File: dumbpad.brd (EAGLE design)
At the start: 97 x 78.5 mm, 41 parts

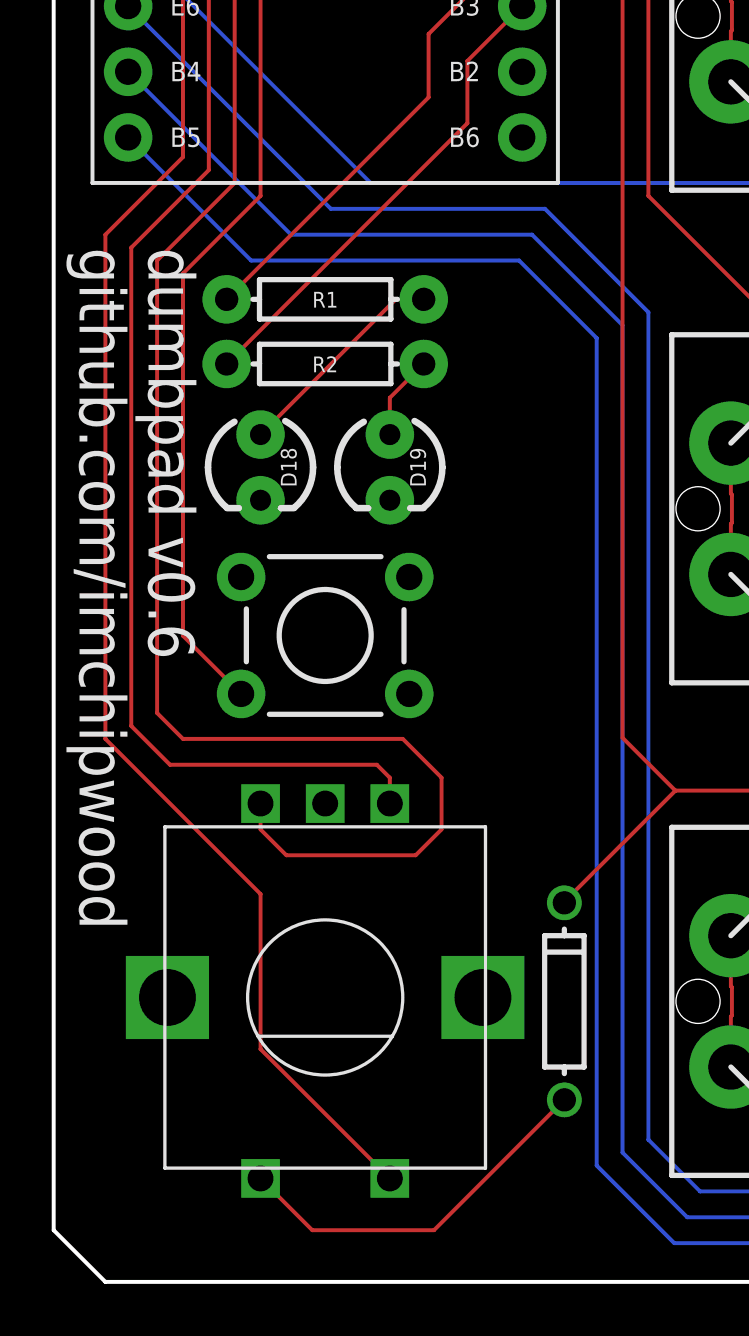
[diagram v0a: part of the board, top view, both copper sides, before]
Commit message: added jumpers for reversing encoder when using encoder on right side instead of left
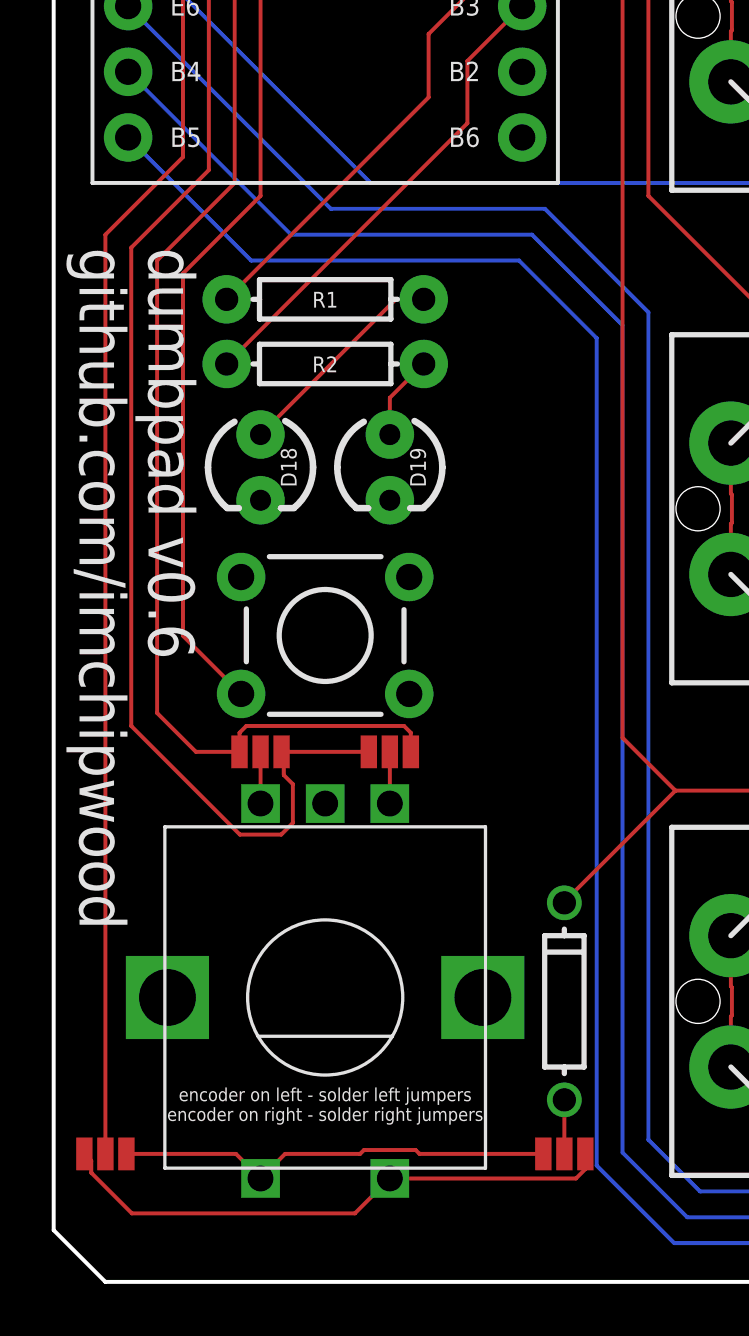
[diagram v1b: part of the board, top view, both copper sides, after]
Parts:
- added JP1, JP2, JP3, JP4: JUMPER-SMT_3_NO_NO-SILK, SparkFun-Jumpers:SMT-JUMPER_3_NO_NO-SILK
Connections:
- removed net N$10: D17.A, RE1.E
- new net ENCODER_A_B: JP3.2, RE1.A
- new net ENCODER_B_A: JP4.2, RE1.B
- new net ROW3_A: D17.A, JP1.2
- new net S17_D: JP1.1, JP2.3, RE1.D
- new net S17_E: JP1.3, JP2.1, RE1.E
- net COL0: now also JP2.2; no longer RE1.D
- net ENCODER_L0: now also JP3.1, JP4.1; no longer RE1.A
- net ENCODER_L1: now also JP3.3, JP4.3; no longer RE1.B
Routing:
- net S17_D: track 0.00 -> 21.9 mm
- net S17_E: track 0.00 -> 17.0 mm
- net N$10: track 14.7 -> 0.00 mm
- net ENCODER_L1: track 63.3 -> 52.6 mm
- net COL0: track 57.1 -> 51.6 mm
- net ENCODER_L0: track 49.8 -> 52.4 mm
- net ROW3_A: track 0.00 -> 2.09 mm
- net ENCODER_B_A: track 0.00 -> 2.00 mm
- net ENCODER_A_B: track 0.00 -> 2.00 mm
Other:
- board text added: "encoder on left - solder left jumpers encoder on right - solder right jumpers"
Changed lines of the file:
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@@
 <?xml version="1.0" encoding="utf-8"?>
 <!DOCTYPE eagle SYSTEM "eagle.dtd">
-<eagle version="9.4.2">
+<eagle version="9.5.2">
 <drawing>
 <settings>
@@
 <setting verticaltext="up"/>
 </settings>
-<grid distance="0.5" unitdist="mm" unit="mm" style="lines" multiple="2" display="yes" altdistance="0.05" altunitdist="mm" altunit="mm"/>
+<grid distance="0.05" unitdist="mm" unit="mm" style="lines" multiple="2" display="yes" altdistance="0.05" altunitdist="mm" altunit="mm"/>
 <layers>
 <layer number="1" name="Top" color="4" fill="1" visible="yes" active="yes"/>
@@
 <layer number="25" name="tNames" color="7" fill="1" visible="yes" active="yes"/>
 <layer number="26" name="bNames" color="7" fill="1" visible="yes" active="yes"/>
-<layer number="27" name="tValues" color="7" fill="1" visible="yes" active="yes"/>
-<layer number="28" name="bValues" color="7" fill="1" visible="yes" active="yes"/>
+<layer number="27" name="tValues" color="7" fill="1" visible="no" active="yes"/>
+<layer number="28" name="bValues" color="7" fill="1" visible="no" active="yes"/>
 <layer number="29" name="tStop" color="7" fill="3" visible="yes" active="yes"/>
 <layer number="30" name="bStop" color="7" fill="6" visible="yes" active="yes"/>
@@
 <wire x1="2" y1="78.5" x2="0" y2="76.5" width="0.1524" layer="20"/>
 <wire x1="0" y1="76.5" x2="0" y2="2" width="0.1524" layer="20"/>
+<text x="10.5" y="7.5" size="0.51" layer="25" align="top-center">encoder on left - solder left jumpers
+encoder on right - solder right jumpers</text>
 </plain>
 <attributes>
@@
 <attribute name="SF_SKU" value="COM-00097" x="10.5" y="25" size="1.778" layer="27" display="off"/>
 </element>
+<element name="JP1" library="SparkFun-Jumpers" package="SMT-JUMPER_3_NO_NO-SILK" value="JUMPER-SMT_3_NO_NO-SILK" x="19.75" y="4.95" smashed="yes" rot="R180"/>
+<element name="JP2" library="SparkFun-Jumpers" package="SMT-JUMPER_3_NO_NO-SILK" value="JUMPER-SMT_3_NO_NO-SILK" x="2" y="4.95" smashed="yes" rot="R180"/>
+<element name="JP3" library="SparkFun-Jumpers" package="SMT-JUMPER_3_NO_NO-SILK" value="JUMPER-SMT_3_NO_NO-SILK" x="13" y="20.5" smashed="yes">
+<attribute name="VALUE" x="13" y="19.357" size="0.6096" layer="27" font="vector" ratio="20" align="top-center"/>
+</element>
+<element name="JP4" library="SparkFun-Jumpers" package="SMT-JUMPER_3_NO_NO-SILK" value="JUMPER-SMT_3_NO_NO-SILK" x="8" y="20.5" smashed="yes" rot="R180">
+<attribute name="VALUE" x="8" y="21.643" size="0.6096" layer="27" font="vector" ratio="20" rot="R180" align="top-center"/>
+</element>
 </elements>
 <signals>
@@
 </signal>
 <signal name="ENCODER_L0">
-<contactref element="RE1" pad="A"/>
 <contactref element="B1" pad="7"/>
-<wire x1="13" y1="18.5" x2="13" y2="19.5" width="0.1524" layer="1"/>
-<wire x1="13" y1="19.5" x2="12.5" y2="20" width="0.1524" layer="1"/>
-<wire x1="4.5" y1="20" x2="3" y2="21.5" width="0.1524" layer="1"/>
-<wire x1="12.5" y1="20" x2="4.5" y2="20" width="0.1524" layer="1"/>
-<wire x1="3" y1="21.5" x2="3" y2="40" width="0.1524" layer="1"/>
+<wire x1="3" y1="40" x2="3" y2="21.5" width="0.1524" layer="1"/>
 <wire x1="3" y1="40" x2="6" y2="43" width="0.1524" layer="1"/>
 <wire x1="6" y1="43" x2="6" y2="53.84" width="0.1524" layer="1"/>
 <wire x1="6" y1="53.84" x2="2.88" y2="56.96" width="0.1524" layer="1"/>
+<contactref element="JP3" pad="1"/>
+<contactref element="JP4" pad="1"/>
+<wire x1="8.8128" y1="20.5" x2="8.9" y2="20.5" width="0.1524" layer="1"/>
+<wire x1="8.9" y1="20.5" x2="12.1872" y2="20.5" width="0.1524" layer="1"/>
+<wire x1="8.8" y1="17.3" x2="9.25" y2="17.75" width="0.1524" layer="1"/>
+<wire x1="9.25" y1="17.75" x2="9.25" y2="19.25" width="0.1524" layer="1"/>
+<wire x1="8.9" y1="19.6" x2="8.9" y2="20.5" width="0.1524" layer="1"/>
+<wire x1="3" y1="21.5" x2="7.2" y2="17.3" width="0.1524" layer="1"/>
+<wire x1="7.2" y1="17.3" x2="8.8" y2="17.3" width="0.1524" layer="1"/>
+<wire x1="9.25" y1="19.25" x2="8.9" y2="19.6" width="0.1524" layer="1"/>
 </signal>
 <signal name="ENCODER_L1">
 <contactref element="B1" pad="6"/>
-<contactref element="RE1" pad="B"/>
-<wire x1="14" y1="16.5" x2="15" y2="17.5" width="0.1524" layer="1"/>
-<wire x1="14" y1="16.5" x2="9" y2="16.5" width="0.1524" layer="1"/>
-<wire x1="9" y1="16.5" x2="8" y2="17.5" width="0.1524" layer="1"/>
-<wire x1="8" y1="17.5" x2="8" y2="18.5" width="0.1524" layer="1"/>
 <wire x1="4" y1="39.5" x2="7" y2="42.5" width="0.1524" layer="1"/>
 <wire x1="7" y1="42.5" x2="7" y2="55.38" width="0.1524" layer="1"/>
 <wire x1="7" y1="55.38" x2="2.88" y2="59.5" width="0.1524" layer="1"/>
-<wire x1="15" y1="19.5" x2="13.5" y2="21" width="0.1524" layer="1"/>
-<wire x1="5" y1="21" x2="4" y2="22" width="0.1524" layer="1"/>
-<wire x1="15" y1="17.5" x2="15" y2="19.5" width="0.1524" layer="1"/>
-<wire x1="13.5" y1="21" x2="5" y2="21" width="0.1524" layer="1"/>
-<wire x1="4" y1="22" x2="4" y2="39.5" width="0.1524" layer="1"/>
+<wire x1="4" y1="39.5" x2="4" y2="22" width="0.1524" layer="1"/>
+<contactref element="JP3" pad="3"/>
+<contactref element="JP4" pad="3"/>
+<wire x1="5.5" y1="20.5" x2="7.1872" y2="20.5" width="0.1524" layer="1"/>
+<wire x1="4" y1="22" x2="5.5" y2="20.5" width="0.1524" layer="1"/>
+<wire x1="7.1872" y1="20.5" x2="7.1872" y2="21.2372" width="0.1524" layer="1"/>
+<wire x1="7.1872" y1="21.2372" x2="7.45" y2="21.5" width="0.1524" layer="1"/>
+<wire x1="13.8128" y1="21.2372" x2="13.8128" y2="20.5" width="0.1524" layer="1"/>
+<wire x1="7.45" y1="21.5" x2="13.55" y2="21.5" width="0.1524" layer="1"/>
+<wire x1="13.55" y1="21.5" x2="13.8128" y2="21.2372" width="0.1524" layer="1"/>
 </signal>
 <signal name="ROW0">
@@
 </signal>
 <signal name="COL0">
-<contactref element="RE1" pad="D"/>
 <contactref element="B1" pad="8"/>
-<wire x1="13" y1="4" x2="8" y2="9" width="0.1524" layer="1"/>
-<wire x1="8" y1="15" x2="2" y2="21" width="0.1524" layer="1"/>
-<wire x1="8" y1="9" x2="8" y2="15" width="0.1524" layer="1"/>
-<wire x1="2" y1="21" x2="2" y2="40.5" width="0.1524" layer="1"/>
-<wire x1="2" y1="40.5" x2="5" y2="43.5" width="0.1524" layer="1"/>
+<wire x1="5" y1="43.5" x2="2" y2="40.5" width="0.1524" layer="1"/>
 <wire x1="5" y1="43.5" x2="5" y2="52.3" width="0.1524" layer="1"/>
 <wire x1="5" y1="52.3" x2="2.88" y2="54.42" width="0.1524" layer="1"/>
+<contactref element="JP2" pad="2"/>
+<wire x1="2" y1="40.5" x2="2" y2="4.95" width="0.1524" layer="1"/>
 </signal>
 <signal name="COL1">
@@
 <wire x1="5" y1="39" x2="5" y2="24.9882" width="0.1524" layer="1"/>
 </signal>
-<signal name="N$10">
-<contactref element="D17" pad="A"/>
-<contactref element="RE1" pad="E"/>
-<wire x1="8" y1="4" x2="10" y2="2" width="0.1524" layer="1"/>
-<wire x1="14.71" y1="2" x2="19.75" y2="7.04" width="0.1524" layer="1"/>
-<wire x1="10" y1="2" x2="14.71" y2="2" width="0.1524" layer="1"/>
-</signal>
 <signal name="COL4">
 <contactref element="S16" pad="S2_0"/>
@@
 <wire x1="16" y1="44.81" x2="16" y2="47.22" width="0.1524" layer="1"/>
 </signal>
+<signal name="S17_E">
+<contactref element="JP1" pad="3"/>
+<contactref element="RE1" pad="E"/>
+<contactref element="JP2" pad="1"/>
+<wire x1="8" y1="4" x2="8.95" y2="4.95" width="0.1524" layer="1"/>
+<wire x1="8.95" y1="4.95" x2="11.85" y2="4.95" width="0.1524" layer="1"/>
+<wire x1="11.85" y1="4.95" x2="12" y2="5.1" width="0.1524" layer="1"/>
+<wire x1="12" y1="5.1" x2="14" y2="5.1" width="0.1524" layer="1"/>
+<wire x1="14" y1="5.1" x2="14.15" y2="4.95" width="0.1524" layer="1"/>
+<wire x1="8" y1="4" x2="7.05" y2="4.95" width="0.1524" layer="1"/>
+<wire x1="7.05" y1="4.95" x2="2.8128" y2="4.95" width="0.1524" layer="1"/>
+<wire x1="14.15" y1="4.95" x2="18.9372" y2="4.95" width="0.1524" layer="1"/>
+</signal>
+<signal name="S17_D">
+<contactref element="RE1" pad="D"/>
+<contactref element="JP1" pad="1"/>
+<contactref element="JP2" pad="3"/>
+<wire x1="20.5628" y1="4.95" x2="20.5628" y2="4.3628" width="0.1524" layer="1"/>
+<wire x1="20.2" y1="4" x2="20.5628" y2="4.3628" width="0.1524" layer="1"/>
+<wire x1="20.2" y1="4" x2="13" y2="4" width="0.1524" layer="1"/>
+<wire x1="1.1872" y1="4.95" x2="1.4539" y2="4.6833" width="0.1524" layer="1"/>
+<wire x1="1.4539" y1="4.6833" x2="1.4539" y2="4.2203125" width="0.1524" layer="1"/>
+<wire x1="1.4539" y1="4.2203125" x2="3.0242125" y2="2.65" width="0.1524" layer="1"/>
+<wire x1="11.65" y1="2.65" x2="13" y2="4" width="0.1524" layer="1"/>
+<wire x1="3.0242125" y1="2.65" x2="11.65" y2="2.65" width="0.1524" layer="1"/>
+</signal>
+<signal name="ROW3_A">
+<contactref element="D17" pad="A"/>
+<contactref element="JP1" pad="2"/>
+<wire x1="19.75" y1="7.04" x2="19.75" y2="4.95" width="0.1524" layer="1"/>
+</signal>
+<signal name="ENCODER_A_B">
+<contactref element="RE1" pad="A"/>
+<contactref element="JP3" pad="2"/>
+<wire x1="13" y1="20.5" x2="13" y2="18.5" width="0.1524" layer="1"/>
+</signal>
+<signal name="ENCODER_B_A">
+<contactref element="RE1" pad="B"/>
+<contactref element="JP4" pad="2"/>
+<wire x1="8" y1="20.5" x2="8" y2="18.5" width="0.1524" layer="1"/>
+</signal>
 </signals>

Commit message: updated revision to v0.7
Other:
- board text added: "dumbpad v0.7 github.com/imchipwood"
- board text removed: "dumbpad v0.6 github.com/imchipwood"
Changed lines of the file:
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@@
 <board>
 <plain>
-<text x="1" y="40" size="1.778" layer="25" rot="SR270">dumbpad v0.6
+<text x="1" y="40" size="1.778" layer="25" rot="SR270">dumbpad v0.7
 github.com/imchipwood</text>
 <wire x1="1.5" y1="76" x2="6.5" y2="76" width="0.1524" layer="21"/>
@@
 <wire x1="14.5" y1="77.5" x2="14.5" y2="76" width="0.1524" layer="21"/>
 <text x="10.5" y="73.5" size="1.778" layer="21" align="bottom-center">pro micro</text>
-<text x="1" y="15" size="1.778" layer="26" rot="SMR90">dumbpad v0.6
+<text x="1" y="15" size="1.778" layer="26" rot="SMR90">dumbpad v0.7
 github.com/imchipwood</text>
 <text x="16.5" y="69.67" size="0.75" layer="21" align="center-right">GND</text>

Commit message: merging v08_jumpers to master
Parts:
- removed JP3, JP4: JUMPER-SMT_3_NO_NO-SILK, SparkFun-Jumpers:SMT-JUMPER_3_NO_NO-SILK
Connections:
- removed net ENCODER_A_B: JP3.2, RE1.A
- removed net ENCODER_B_A: JP4.2, RE1.B
- net ENCODER_L0: now also RE1.A; no longer JP3.1, JP4.1
- net ENCODER_L1: now also RE1.B; no longer JP3.3, JP4.3
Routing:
- net ENCODER_L1: track 52.6 -> 45.9 mm
- net ENCODER_L0: track 52.4 -> 50.2 mm
- net ENCODER_B_A: track 2.00 -> 0.00 mm
- net ENCODER_A_B: track 2.00 -> 0.00 mm
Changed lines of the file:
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@@
 <element name="JP1" library="SparkFun-Jumpers" package="SMT-JUMPER_3_NO_NO-SILK" value="JUMPER-SMT_3_NO_NO-SILK" x="19.75" y="4.95" smashed="yes" rot="R180"/>
 <element name="JP2" library="SparkFun-Jumpers" package="SMT-JUMPER_3_NO_NO-SILK" value="JUMPER-SMT_3_NO_NO-SILK" x="2" y="4.95" smashed="yes" rot="R180"/>
-<element name="JP3" library="SparkFun-Jumpers" package="SMT-JUMPER_3_NO_NO-SILK" value="JUMPER-SMT_3_NO_NO-SILK" x="13" y="20.5" smashed="yes">
-<attribute name="VALUE" x="13" y="19.357" size="0.6096" layer="27" font="vector" ratio="20" align="top-center"/>
-</element>
-<element name="JP4" library="SparkFun-Jumpers" package="SMT-JUMPER_3_NO_NO-SILK" value="JUMPER-SMT_3_NO_NO-SILK" x="8" y="20.5" smashed="yes" rot="R180">
-<attribute name="VALUE" x="8" y="21.643" size="0.6096" layer="27" font="vector" ratio="20" rot="R180" align="top-center"/>
-</element>
 </elements>
 <signals>
@@
 <wire x1="6" y1="43" x2="6" y2="53.84" width="0.1524" layer="1"/>
 <wire x1="6" y1="53.84" x2="2.88" y2="56.96" width="0.1524" layer="1"/>
-<contactref element="JP3" pad="1"/>
-<contactref element="JP4" pad="1"/>
-<wire x1="8.8128" y1="20.5" x2="8.9" y2="20.5" width="0.1524" layer="1"/>
-<wire x1="8.9" y1="20.5" x2="12.1872" y2="20.5" width="0.1524" layer="1"/>
-<wire x1="8.8" y1="17.3" x2="9.25" y2="17.75" width="0.1524" layer="1"/>
-<wire x1="9.25" y1="17.75" x2="9.25" y2="19.25" width="0.1524" layer="1"/>
-<wire x1="8.9" y1="19.6" x2="8.9" y2="20.5" width="0.1524" layer="1"/>
 <wire x1="3" y1="21.5" x2="7.2" y2="17.3" width="0.1524" layer="1"/>
-<wire x1="7.2" y1="17.3" x2="8.8" y2="17.3" width="0.1524" layer="1"/>
-<wire x1="9.25" y1="19.25" x2="8.9" y2="19.6" width="0.1524" layer="1"/>
+<contactref element="RE1" pad="A"/>
+<wire x1="7.2" y1="17.3" x2="11.8" y2="17.3" width="0.1524" layer="1"/>
+<wire x1="11.8" y1="17.3" x2="13" y2="18.5" width="0.1524" layer="1"/>
 </signal>
 <signal name="ENCODER_L1">
@@
 <wire x1="7" y1="55.38" x2="2.88" y2="59.5" width="0.1524" layer="1"/>
 <wire x1="4" y1="39.5" x2="4" y2="22" width="0.1524" layer="1"/>
-<contactref element="JP3" pad="3"/>
-<contactref element="JP4" pad="3"/>
-<wire x1="5.5" y1="20.5" x2="7.1872" y2="20.5" width="0.1524" layer="1"/>
-<wire x1="4" y1="22" x2="5.5" y2="20.5" width="0.1524" layer="1"/>
-<wire x1="7.1872" y1="20.5" x2="7.1872" y2="21.2372" width="0.1524" layer="1"/>
-<wire x1="7.1872" y1="21.2372" x2="7.45" y2="21.5" width="0.1524" layer="1"/>
-<wire x1="13.8128" y1="21.2372" x2="13.8128" y2="20.5" width="0.1524" layer="1"/>
-<wire x1="7.45" y1="21.5" x2="13.55" y2="21.5" width="0.1524" layer="1"/>
-<wire x1="13.55" y1="21.5" x2="13.8128" y2="21.2372" width="0.1524" layer="1"/>
+<contactref element="RE1" pad="B"/>
+<wire x1="7.5" y1="18.5" x2="8" y2="18.5" width="0.1524" layer="1"/>
+<wire x1="4" y1="22" x2="7.5" y2="18.5" width="0.1524" layer="1"/>
 </signal>
 <signal name="ROW0">
@@
 <wire x1="19.75" y1="7.04" x2="19.75" y2="4.95" width="0.1524" layer="1"/>
 </signal>
-<signal name="ENCODER_A_B">
-<contactref element="RE1" pad="A"/>
-<contactref element="JP3" pad="2"/>
-<wire x1="13" y1="20.5" x2="13" y2="18.5" width="0.1524" layer="1"/>
-</signal>
-<signal name="ENCODER_B_A">
-<contactref element="RE1" pad="B"/>
-<contactref element="JP4" pad="2"/>
-<wire x1="8" y1="20.5" x2="8" y2="18.5" width="0.1524" layer="1"/>
-</signal>
 </signals>
